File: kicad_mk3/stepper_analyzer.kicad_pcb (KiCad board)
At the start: 2 copper layers, 102 x 57 mm, 22 parts, among them J1 Connector_Conn_01x04_Male, J2 Connector_Conn_01x04_Male, M1 Motor, Q1 AO3400A, U1 ACS70331EOLCTR-2P5B3, U2 ACS70331EOLCTR-2P5B3, U3 Pico

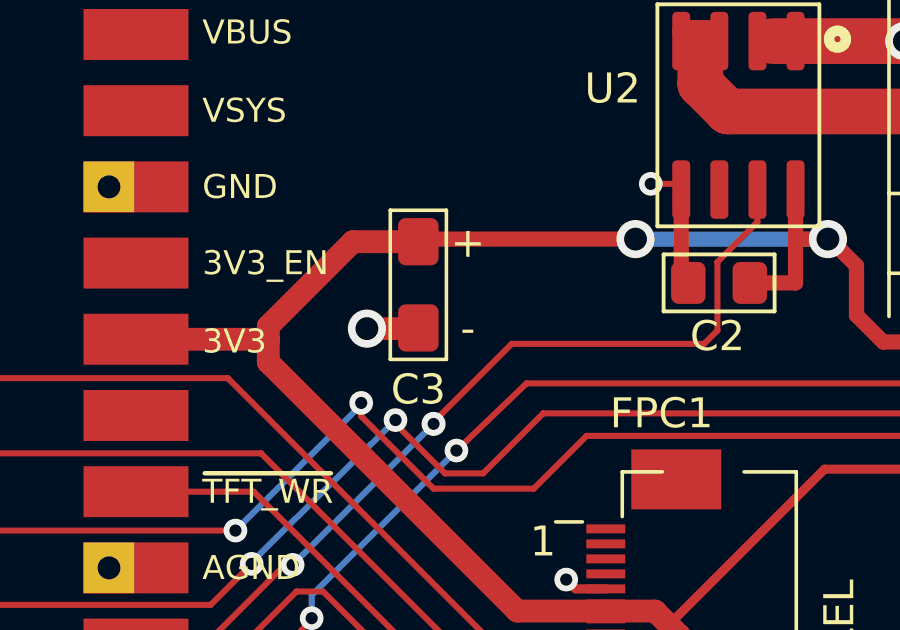
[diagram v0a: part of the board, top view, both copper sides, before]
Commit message: Changed 10u from tant to ceramic.
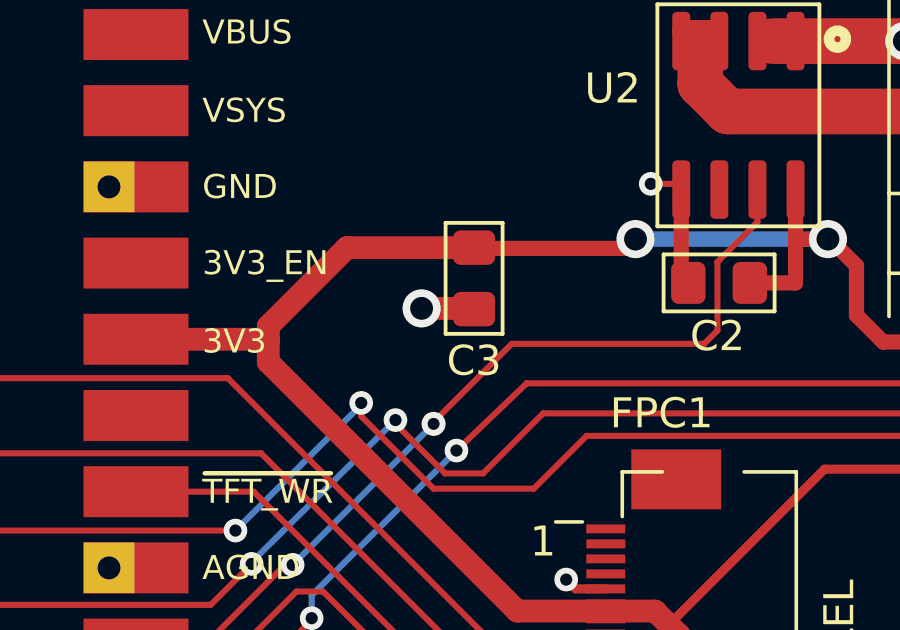
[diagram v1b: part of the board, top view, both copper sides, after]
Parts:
- C3: footprint stepper_motor_analyzer:CP_EIA-3216-18_Kemet-A_Pad1.58x1.35mm_HandSolder -> stepper_motor_analyzer:C_0805_2012Metric_Pad1.15x1.40mm_HandSolder
- moved C3 1.87 mm to (44.1, -47.0), turned to 90 degrees
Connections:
- C3 pad 1: +3V3 -> GND
- C3 pad 2: GND -> +3V3
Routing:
- net GND: track 45.2 -> 44.6 mm
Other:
- board text removed: "+"
- board text removed: "-"

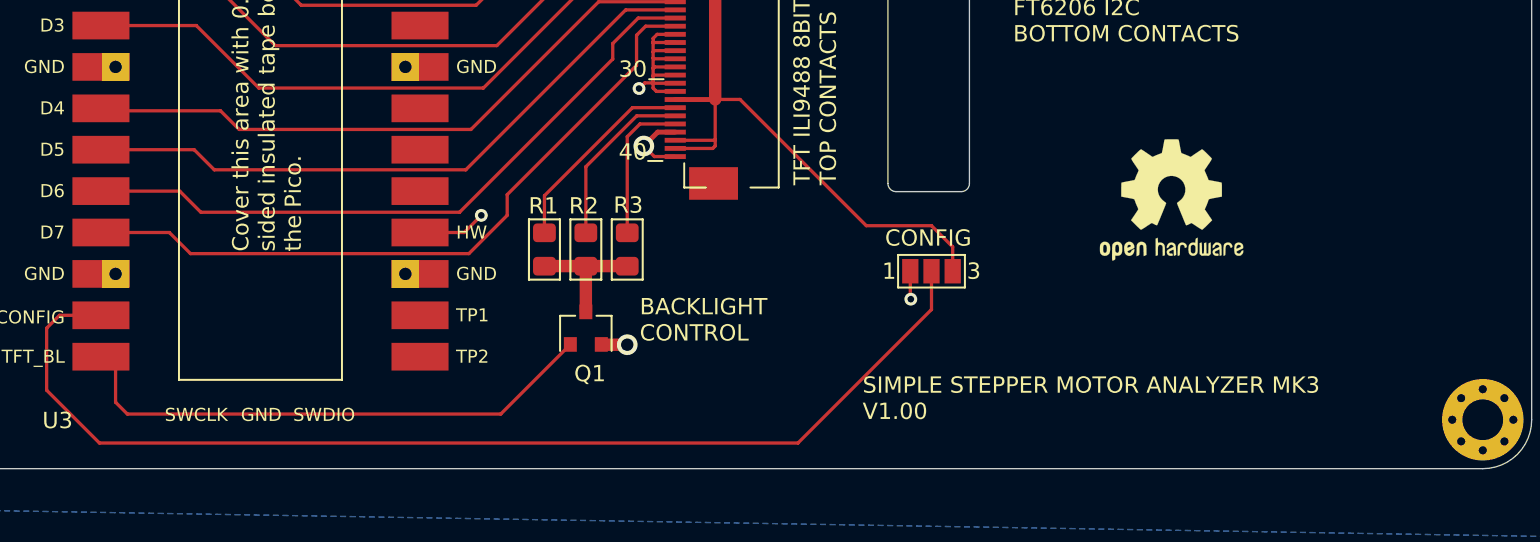
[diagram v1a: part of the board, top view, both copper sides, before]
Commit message: Change config jumpers to resistors.
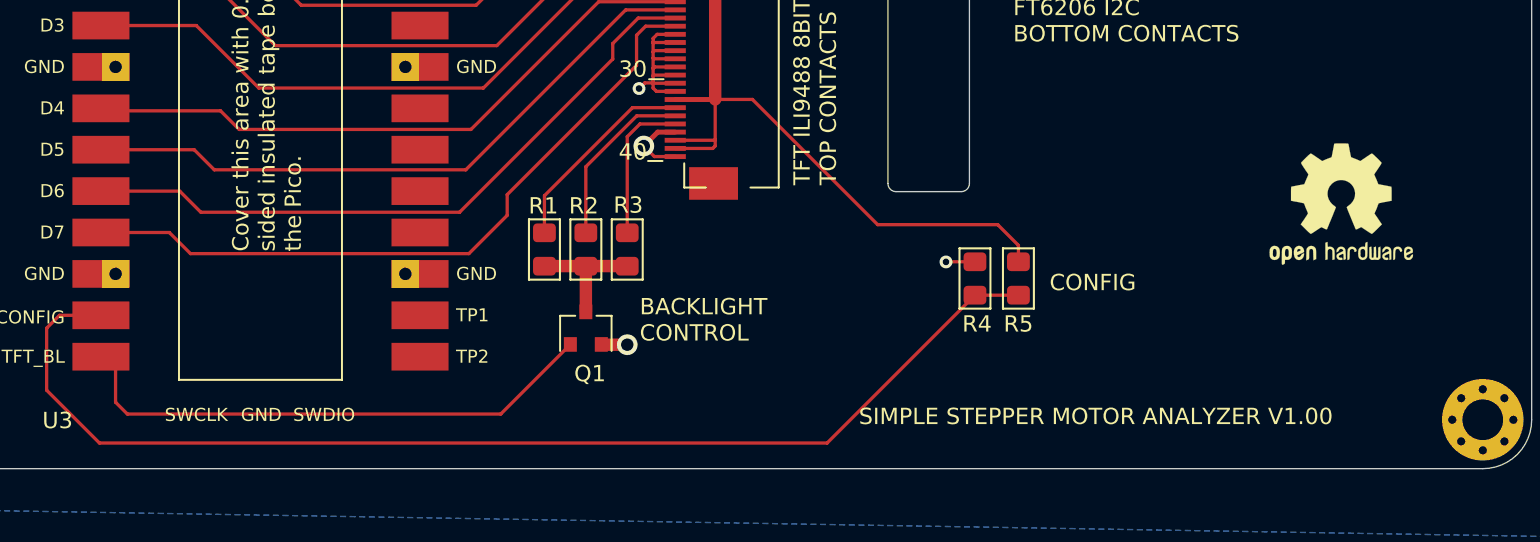
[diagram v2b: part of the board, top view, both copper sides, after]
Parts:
- removed JP1: SolderJumper_3_Open, Jumper:SolderJumper-3_P1.3mm_Open_Pad1.0x1.5mm_NumberLabels
- added R4: DNP, stepper_motor_analyzer:R_0805_2012Metric_Pad1.15x1.40mm_HandSolder, F.Cu at (66.8, -11.7)
- added R5: DNP, stepper_motor_analyzer:R_0805_2012Metric_Pad1.15x1.40mm_HandSolder, F.Cu at (69.5, -11.7)
- moved LOGO1 10.4 mm to (89.3, -16.2)
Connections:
- U3 pad 24: GND -> Net-(U3-Pad24)
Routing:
- net GND: track 44.6 -> 39.6 mm, vias 13 -> 12
- net +3V3: track 161.7 -> 165.2 mm
- net /CONFIG: track 69.7 -> 73.1 mm
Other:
- board text added: "SIMPLE STEPPER MOTOR ANALYZER V1.00"
- board text removed: "SIMPLE STEPPER MOTOR ANALYZER MK3 V1.00"
